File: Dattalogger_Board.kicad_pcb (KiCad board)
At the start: 2 copper layers, 0 parts

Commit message: Completed Placments of footprints and sizing the board
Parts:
- added BT1: Battery, Connector_PinHeader_2.54mm:PinHeader_2x01_P2.54mm_Vertical, F.Cu at (131.4, 73.7)
- added C1: 0.1uF, Capacitor_SMD:C_0805_2012Metric, F.Cu at (148.0, 66.2)
- added C2: 22pF, Capacitor_SMD:C_0805_2012Metric, F.Cu at (161.9, 79.4)
- added C3: 22pF, Capacitor_SMD:C_0805_2012Metric, F.Cu at (152.4, 66.0)
- added C4: 0.1uF, Capacitor_SMD:C_0805_2012Metric, F.Cu at (161.9, 83.2)
- added C5: 100nF, Capacitor_SMD:C_0805_2012Metric, F.Cu at (156.8, 66.0)
- added D1: LED, LED_SMD:LED_0805_2012Metric, F.Cu at (165.7, 66.0)
- added D2: LED, LED_SMD:LED_0805_2012Metric, F.Cu at (161.9, 66.0)
- added H1: MountingHole, MountingHole:MountingHole_2.1mm, F.Cu at (130.2, 67.3)
- added H2: MountingHole, MountingHole:MountingHole_2.1mm, F.Cu at (130.2, 90.8)
- added H3: MountingHole, MountingHole:MountingHole_2.1mm, F.Cu at (174.6, 67.3)
- added H4: MountingHole, MountingHole:MountingHole_2.1mm, F.Cu at (174.6, 90.8)
- added J1: Conn_01x04_Pin, Connector_PinHeader_2.54mm:PinHeader_1x04_P2.54mm_Vertical, F.Cu at (170.2, 81.3)
- added J2: Conn_01x04_Pin, Connector_PinHeader_2.54mm:PinHeader_1x04_P2.54mm_Vertical, F.Cu at (158.8, 91.4)
- added J3: Conn_02x03_Odd_Even, Connector_PinHeader_2.54mm:PinHeader_2x03_P2.54mm_Vertical, F.Cu at (170.2, 71.8)
- added J4: Conn_01x09_Pin, Connector_PinHeader_2.54mm:PinHeader_1x09_P2.54mm_Vertical, F.Cu at (134.6, 91.4)
- added R1: 10K, Resistor_SMD:R_0805_2012Metric, F.Cu at (138.4, 87.6)
- added R2: 10K, Resistor_SMD:R_0805_2012Metric, F.Cu at (142.2, 87.6)
- added R3: 4.7K, Resistor_SMD:R_0805_2012Metric, F.Cu at (161.9, 76.2)
- added R4: 4.7K, Resistor_SMD:R_0805_2012Metric, F.Cu at (161.9, 73.0)
- added R5: 330, Resistor_SMD:R_0805_2012Metric, F.Cu at (165.7, 69.8)
- added R6: 10K, Resistor_SMD:R_0805_2012Metric, F.Cu at (165.7, 73.0)
- added R7: 330, Resistor_SMD:R_0805_2012Metric, F.Cu at (161.9, 69.8)
- added U1: 24LC1025, Package_SO:SOIC-8_5.23x5.23mm_P1.27mm, F.Cu at (140.3, 75.6)
- added U2: DS1337S_, Project_Libraries:SOIC127P600X175-8N, F.Cu at (140.3, 82.5)
- added U3: 24LC1025, Package_SO:SOIC-8_5.23x5.23mm_P1.27mm, F.Cu at (140.3, 67.9)
- added U4: ATMEGA328P-AU, Project_Libraries:QFP80P900X900X120-32N, F.Cu at (152.4, 78.7)
- added Y1: 32.768 KHz, Crystal:Crystal_SMD_5032-2Pin_5.0x3.2mm_HandSoldering, F.Cu at (131.4, 83.2)
- added Y2: 16 MHz, Crystal:Crystal_SMD_5032-2Pin_5.0x3.2mm_HandSoldering, F.Cu at (152.4, 86.4)

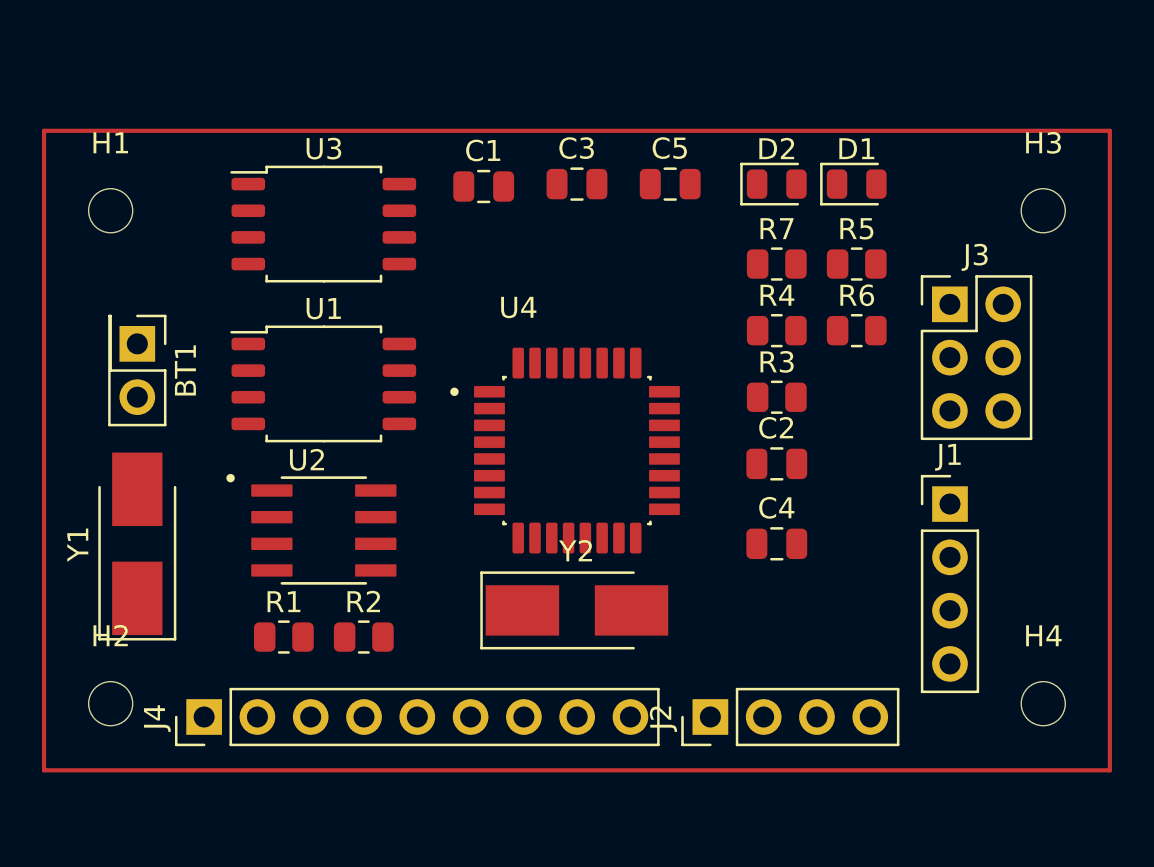
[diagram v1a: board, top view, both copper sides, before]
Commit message: Refined and completed outline
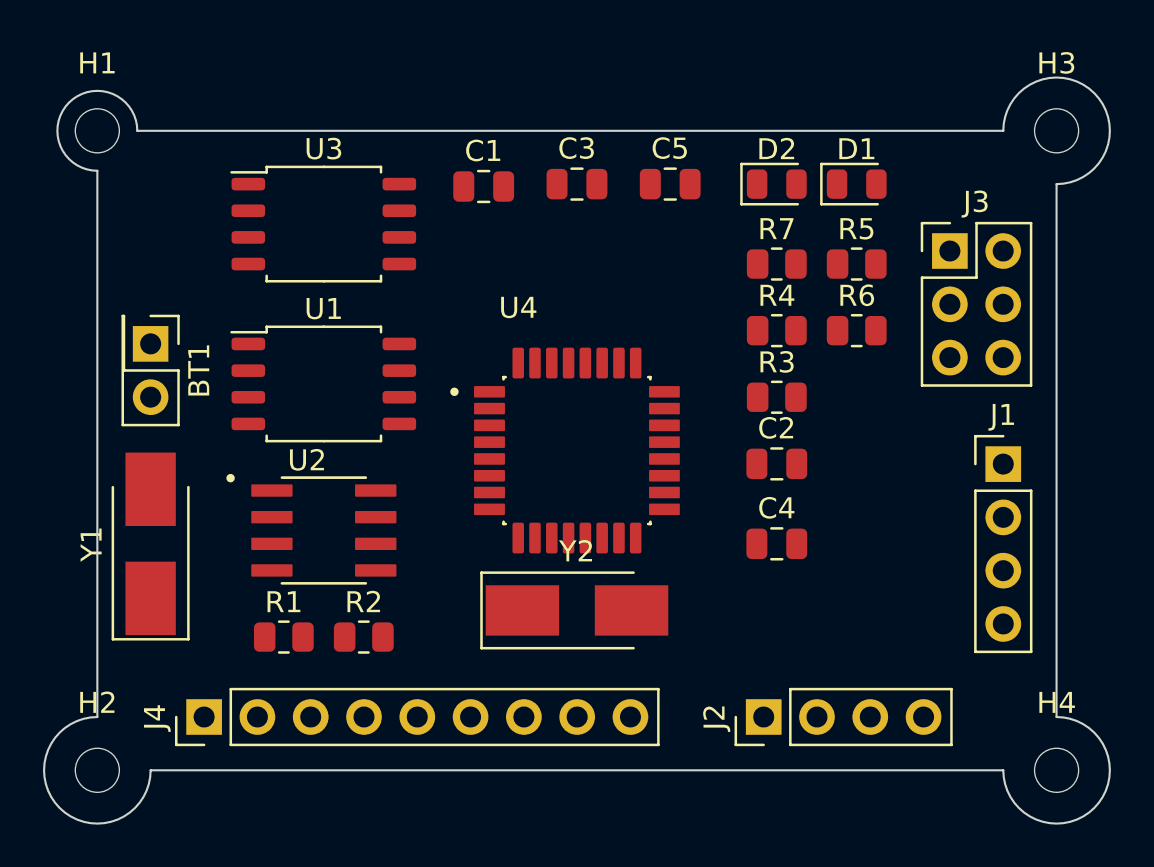
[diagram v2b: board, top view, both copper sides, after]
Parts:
- moved H1 3.86 mm to (129.5, 63.5)
- moved H3 3.86 mm to (175.3, 63.5)
- moved H2 3.24 mm to (129.5, 94.0)
- moved H4 3.24 mm to (175.3, 94.0)
- moved J1 3.17 mm to (172.7, 79.4)
- moved J2 2.54 mm to (161.3, 91.4)
- moved J3 2.54 mm to (170.2, 69.2)
- moved BT1 0.64 mm to (132.1, 73.7)
- moved Y1 0.64 mm to (132.1, 83.2)
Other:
- board outline added: 50.8 x 35.6 mm
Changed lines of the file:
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@@
   (net 34 "unconnected-(U4-PC3-Pad26)")
   (footprint "Connector_PinHeader_2.54mm:PinHeader_1x04_P2.54mm_Vertical" (layer "F.Cu")
-    (at 158.76 91.44 90)
+    (at 161.3 91.44 90)
     (descr "Through hole straight pin header, 1x04, 2.54mm pitch, single row")
     (tags "Through hole pin header THT 1x04 2.54mm single row")
@@
   )
   (footprint "MountingHole:MountingHole_2.1mm" (layer "F.Cu")
-    (at 130.175 67.31)
+    (at 129.54 63.5)
     (descr "Mounting Hole 2.1mm, no annular")
     (tags "mounting hole 2.1mm no annular")
@@
   )
   (footprint "Connector_PinHeader_2.54mm:PinHeader_2x03_P2.54mm_Vertical" (layer "F.Cu")
-    (at 170.175 71.77)
+    (at 170.175 69.23)
     (descr "Through hole straight pin header, 2x03, 2.54mm pitch, double rows")
     (tags "Through hole pin header THT 2x03 2.54mm double row")
@@
         (effects (font (size 1 1) (thickness 0.15)))
     )
-    (fp_text value "Conn_02x03_Odd_Even" (at 1.27 7.41) (layer "F.Fab")
+    (fp_text value "Conn_02x03_Odd_Even" (at -1.27 7.41) (layer "F.Fab")
         (effects (font (size 1 1) (thickness 0.15)))
     )
@@
   )
   (footprint "Connector_PinHeader_2.54mm:PinHeader_2x01_P2.54mm_Vertical" (layer "F.Cu")
-    (at 131.445 73.655 -90)
+    (at 132.08 73.655 -90)
     (descr "Through hole straight pin header, 2x01, 2.54mm pitch, double rows")
     (tags "Through hole pin header THT 2x01 2.54mm double row")
@@
   )
   (footprint "MountingHole:MountingHole_2.1mm" (layer "F.Cu")
-    (at 130.175 90.805)
+    (at 129.54 93.98)
     (descr "Mounting Hole 2.1mm, no annular")
     (tags "mounting hole 2.1mm no annular")
@@
   )
   (footprint "Connector_PinHeader_2.54mm:PinHeader_1x04_P2.54mm_Vertical" (layer "F.Cu")
-    (at 170.18 81.29)
+    (at 172.72 79.385)
     (descr "Through hole straight pin header, 1x04, 2.54mm pitch, single row")
     (tags "Through hole pin header THT 1x04 2.54mm single row")
@@
         (effects (font (size 1 1) (thickness 0.15)))
     )
-    (fp_text value "Conn_01x04_Pin" (at 0 9.95) (layer "F.Fab")
+    (fp_text value "Conn_01x04_Pin" (at -2.54 9.95) (layer "F.Fab")
         (effects (font (size 1 1) (thickness 0.15)))
     )
@@
   )
   (footprint "MountingHole:MountingHole_2.1mm" (layer "F.Cu")
-    (at 174.625 90.805)
+    (at 175.26 93.98)
     (descr "Mounting Hole 2.1mm, no annular")
     (tags "mounting hole 2.1mm no annular")
@@
   )
   (footprint "MountingHole:MountingHole_2.1mm" (layer "F.Cu")
-    (at 174.625 67.31)
+    (at 175.26 63.5)
     (descr "Mounting Hole 2.1mm, no annular")
     (tags "mounting hole 2.1mm no annular")
@@
   )
   (footprint "Crystal:Crystal_SMD_5032-2Pin_5.0x3.2mm_HandSoldering" (layer "F.Cu")
-    (at 131.445 83.185 90)
+    (at 132.08 83.185 90)
     (descr "SMD Crystal SERIES SMD2520/2 http://www.icbase.com/File/PDF/HKC/HKC00061008.pdf, hand-soldering, 5.0x3.2mm^2 package")
     (tags "SMD SMT crystal hand-soldering")
@@
     )
   )
-  (gr_rect (start 127 63.5) (end 177.8 93.98)
-    (stroke (width 0.2) (type default)) (fill none) (layer "F.Cu"))
+  (gr_line (start 132.08 93.98) (end 172.72 93.98)
+    (stroke (width 0.1) (type default)) (layer "Edge.Cuts"))
+  (gr_arc (start 129.54 65.405) (mid 128.192962 62.152962) (end 131.445 63.5)
+    (stroke (width 0.1) (type default)) (layer "Edge.Cuts"))
+  (gr_arc (start 132.08 93.98) (mid 127.743949 95.776051) (end 129.54 91.44)
+    (stroke (width 0.1) (type default)) (layer "Edge.Cuts"))
+  (gr_arc (start 175.26 91.44) (mid 177.056051 95.776051) (end 172.72 93.98)
+    (stroke (width 0.1) (type default)) (layer "Edge.Cuts"))
+  (gr_line (start 129.54 91.44) (end 129.54 65.405)
+    (stroke (width 0.1) (type default)) (layer "Edge.Cuts"))
+  (gr_line (start 131.445 63.5) (end 172.72 63.5)
+    (stroke (width 0.1) (type default)) (layer "Edge.Cuts"))
+  (gr_line (start 175.26 91.44) (end 175.26 66.04)
+    (stroke (width 0.1) (type default)) (layer "Edge.Cuts"))
+  (gr_arc (start 172.72 63.5) (mid 177.056051 61.703949) (end 175.26 66.04)
+    (stroke (width 0.1) (type default)) (layer "Edge.Cuts"))
 )

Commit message: Completed Routing
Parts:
- moved C2 4.49 mm to (161.3, 83.8), turned to 180 degrees
- moved C4 3.86 mm to (161.3, 87.0), turned to 180 degrees
- moved R5 3.81 mm to (161.9, 69.8)
- moved R7 3.81 mm to (165.7, 69.8), turned to 180 degrees
- moved U4 1.91 mm to (152.4, 76.8)
- moved R1 0.90 mm to (137.8, 87.0)
- moved R2 0.90 mm to (141.6, 87.0), turned to 180 degrees
- turned R3 to 180 degrees
- turned R4 to 180 degrees
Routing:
- net /Vcc: track 0.00 -> 156.9 mm, vias 0 -> 2
- net GND: track 0.00 -> 145.9 mm, vias 0 -> 8
- net /SCK: track 0.00 -> 99.2 mm, vias 0 -> 3
- net Net-(BT1-+): track 0.00 -> 90.4 mm, vias 0 -> 5
- net /SDA: track 0.00 -> 64.3 mm, vias 0 -> 4
- net Net-(U4-PB7): track 0.00 -> 30.8 mm, vias 0 -> 2
- net /TX: track 0.00 -> 29.0 mm, vias 0 -> 1
- net /D2: track 0.00 -> 27.4 mm, vias 0 -> 1
- net /RX: track 0.00 -> 27.1 mm, vias 0 -> 1
- net /MOSI: track 0.00 -> 24.8 mm
- net /D3: track 0.00 -> 24.6 mm
- net Net-(U4-PB6): track 0.00 -> 24.2 mm
- net /MISO: track 0.00 -> 23.7 mm, vias 0 -> 1
- net /RESET: track 0.00 -> 22.9 mm, vias 0 -> 2
- net /D4: track 0.00 -> 22.4 mm
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- added copper zone on F.Cu, net /Vcc
- added copper zone on B.Cu, net GND

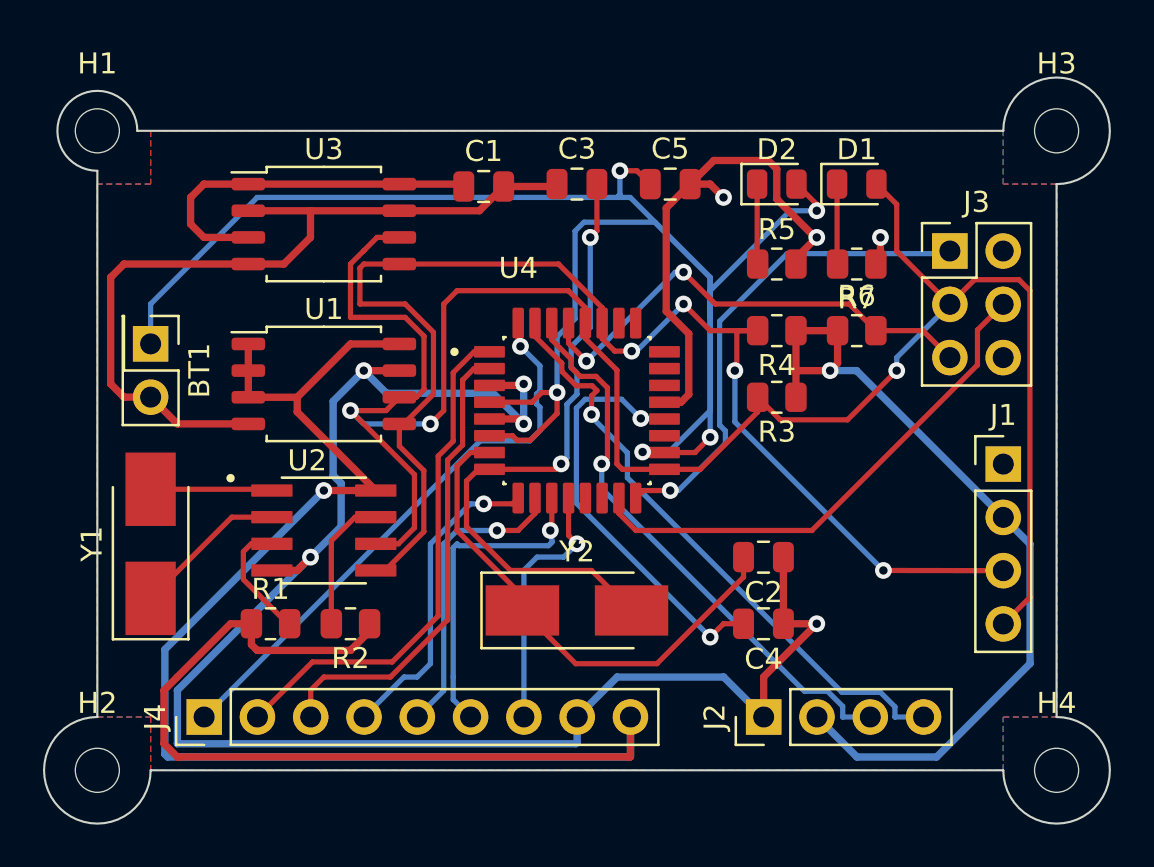
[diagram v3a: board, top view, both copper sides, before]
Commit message: Completed the 2-layer board
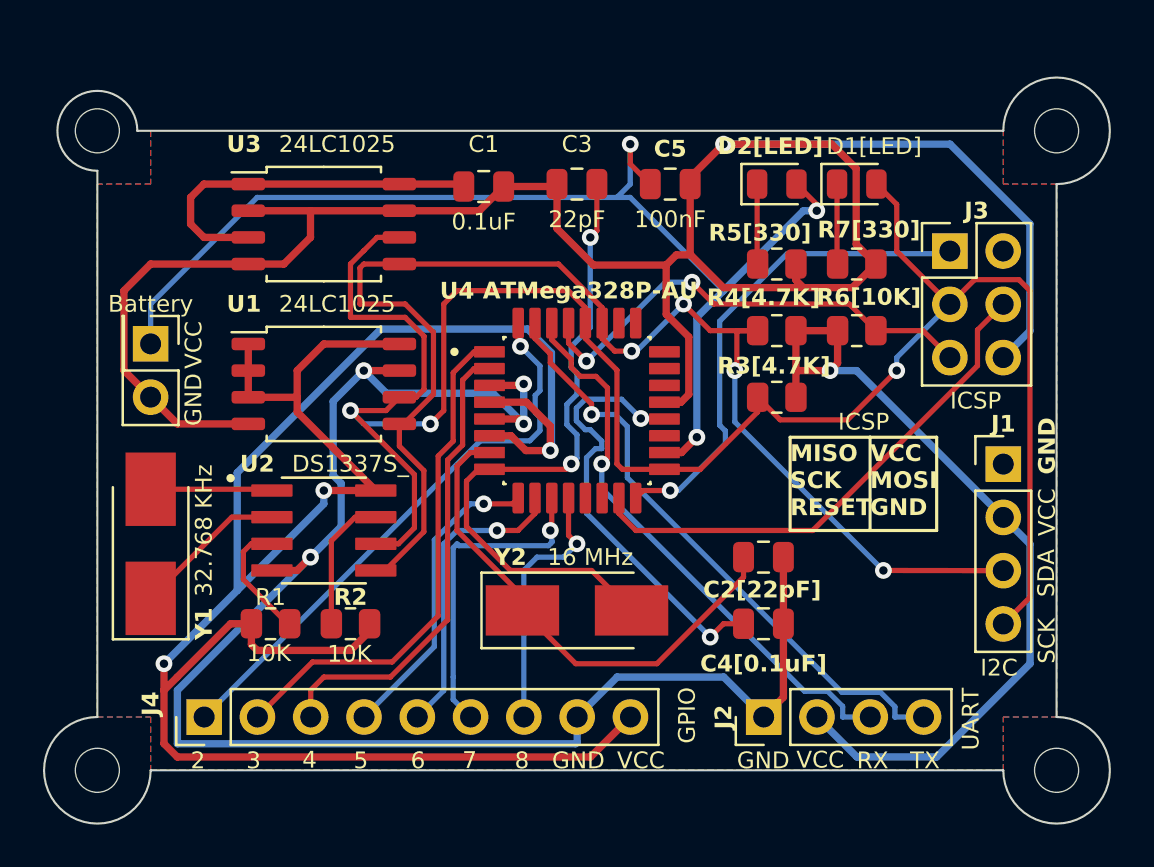
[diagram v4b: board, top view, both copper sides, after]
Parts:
- added Majed: LOGO, Library2:MajedDev, B.Cu at (160.7, 76.2)
- U4: value ATMEGA328P-AU -> ATMega328P-AU
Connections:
- BT1 pad 1: Net-(BT1-+) -> /Vcc
- C5 pad 1: Net-(BT1-+) -> /Vcc
- D2 pad 2: Net-(BT1-+) -> /Vcc
- U4 pad 18: Net-(BT1-+) -> /Vcc
- U4 pad 4: Net-(BT1-+) -> /Vcc
- U4 pad 6: Net-(BT1-+) -> /Vcc
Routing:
- net Net-(BT1-+): track 90.4 -> 0.00 mm, vias 5 -> 0
- net /Vcc: track 156.9 -> 221.0 mm, vias 2 -> 7
- net GND: track 145.9 -> 185.0 mm, vias 8 -> 5
- net Net-(U4-AREF): track 20.2 -> 21.1 mm
- net Net-(U4-PB7): track 30.8 -> 31.5 mm
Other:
- board text added: "2"
- board text added: "3"
- board text added: "4"
- board text added: "5"
- board text added: "6"
- board text added: "7"
- board text added: "8"
- board text added: "C2[22pF]"
- board text added: "C3"
- board text added: "C4[0.1uF]"
- board text added: "D1[LED]"
- board text added: "D2[LED]"
- board text added: "GND"
- board text added: "GPIO"
- board text added: "I2C"
- board text added: "ICSP"
- board text added: "MCU Data Logger For AtMega 328P - 2Mbit EEPROM - RTC - I2C, SPI, GPIOs"
- board text added: "MISO SCK RESET"
- board text added: "R3[4.7K]"
- board text added: "R4[4.7K]"
- board text added: "R5[330]"
- board text added: "R6[10K]"
- board text added: "R7[330]"
- board text added: "RX"
- board text added: "SCK"
- board text added: "SDA"
- board text added: "TX"
- board text added: "UART"
- board text added: "VCC"
- board text added: "VCC MOSI GND"
